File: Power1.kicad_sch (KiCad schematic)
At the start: 23 parts, among them U15 IRS2186, U16 IRS2186, U17 IRS2186, U18 Opamp_Quad

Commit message: - layout almost finished
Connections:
- net U_GH renamed U1_GH
- net U_GL renamed U1_GL
- net U_PWM_H renamed U1_PWM_H
- net U_PWM_L renamed U1_PWM_L
- net U_U renamed U1_U
- net U_VP renamed U1_VP
- net V_GH renamed V1_GH
- net V_GL renamed V1_GL
- net V_PWM_H renamed V1_PWM_H
- net V_PWM_L renamed V1_PWM_L
- net V_U renamed V1_U
- net V_VP renamed V1_VP
- net W_GH renamed W1_GH
- net W_GL renamed W1_GL
- net W_PWM_H renamed W1_PWM_H
- net W_PWM_L renamed W1_PWM_L
- net W_U renamed W1_U
- net W_VP renamed W1_VP
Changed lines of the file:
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@@
     (stroke (width 0) (type default))
   )
-  (hierarchical_label "U_GH" (shape input) (at 69.85 48.26 0) (fields_autoplaced)
+  (hierarchical_label "U1_GH" (shape input) (at 69.85 48.26 0) (fields_autoplaced)
     (effects (font (size 1.27 1.27)) (justify left))
   )
-  (hierarchical_label "U_GL" (shape input) (at 69.85 60.96 0) (fields_autoplaced)
+  (hierarchical_label "U1_GL" (shape input) (at 69.85 60.96 0) (fields_autoplaced)
     (effects (font (size 1.27 1.27)) (justify left))
   )
-  (hierarchical_label "U_PWM_L" (shape input) (at 54.61 55.88 180) (fields_autoplaced)
+  (hierarchical_label "U1_PWM_L" (shape input) (at 54.61 55.88 180) (fields_autoplaced)
     (effects (font (size 1.524 1.524)) (justify right))
   )
-  (hierarchical_label "V_PWM_L" (shape input) (at 54.61 100.33 180) (fields_autoplaced)
+  (hierarchical_label "V1_PWM_L" (shape input) (at 54.61 100.33 180) (fields_autoplaced)
     (effects (font (size 1.524 1.524)) (justify right))
   )
-  (hierarchical_label "U_U" (shape output) (at 223.52 37.465 180) (fields_autoplaced)
+  (hierarchical_label "U1_U" (shape output) (at 223.52 37.465 180) (fields_autoplaced)
     (effects (font (size 1.524 1.524)) (justify right))
   )
-  (hierarchical_label "V_GH" (shape input) (at 69.85 92.71 0) (fields_autoplaced)
+  (hierarchical_label "V1_GH" (shape input) (at 69.85 92.71 0) (fields_autoplaced)
     (effects (font (size 1.27 1.27)) (justify left))
   )
-  (hierarchical_label "V_GL" (shape input) (at 69.85 105.41 0) (fields_autoplaced)
+  (hierarchical_label "V1_GL" (shape input) (at 69.85 105.41 0) (fields_autoplaced)
     (effects (font (size 1.27 1.27)) (justify left))
   )
-  (hierarchical_label "W_VP" (shape input) (at 261.62 78.105 0) (fields_autoplaced)
+  (hierarchical_label "W1_VP" (shape input) (at 261.62 78.105 0) (fields_autoplaced)
     (effects (font (size 1.524 1.524)) (justify left))
   )
-  (hierarchical_label "V_VP" (shape input) (at 83.82 102.87 0) (fields_autoplaced)
+  (hierarchical_label "V1_VP" (shape input) (at 83.82 102.87 0) (fields_autoplaced)
     (effects (font (size 1.27 1.27)) (justify left))
   )
-  (hierarchical_label "U_VP" (shape input) (at 83.82 58.42 0) (fields_autoplaced)
+  (hierarchical_label "U1_VP" (shape input) (at 83.82 58.42 0) (fields_autoplaced)
     (effects (font (size 1.27 1.27)) (justify left))
   )
-  (hierarchical_label "U_VP" (shape input) (at 261.62 34.925 0) (fields_autoplaced)
+  (hierarchical_label "U1_VP" (shape input) (at 261.62 34.925 0) (fields_autoplaced)
     (effects (font (size 1.524 1.524)) (justify left))
   )
-  (hierarchical_label "V_VP" (shape input) (at 261.62 56.515 0) (fields_autoplaced)
+  (hierarchical_label "V1_VP" (shape input) (at 261.62 56.515 0) (fields_autoplaced)
     (effects (font (size 1.524 1.524)) (justify left))
   )
-  (hierarchical_label "V_PWM_H" (shape input) (at 54.61 97.79 180) (fields_autoplaced)
+  (hierarchical_label "V1_PWM_H" (shape input) (at 54.61 97.79 180) (fields_autoplaced)
     (effects (font (size 1.524 1.524)) (justify right))
   )
-  (hierarchical_label "W_PWM_L" (shape input) (at 54.61 144.78 180) (fields_autoplaced)
+  (hierarchical_label "W1_PWM_L" (shape input) (at 54.61 144.78 180) (fields_autoplaced)
     (effects (font (size 1.524 1.524)) (justify right))
   )
-  (hierarchical_label "U_PWM_H" (shape input) (at 54.61 53.34 180) (fields_autoplaced)
+  (hierarchical_label "U1_PWM_H" (shape input) (at 54.61 53.34 180) (fields_autoplaced)
     (effects (font (size 1.524 1.524)) (justify right))
   )
-  (hierarchical_label "W_GL" (shape input) (at 69.85 149.86 0) (fields_autoplaced)
+  (hierarchical_label "W1_GL" (shape input) (at 69.85 149.86 0) (fields_autoplaced)
     (effects (font (size 1.27 1.27)) (justify left))
   )
-  (hierarchical_label "V_U" (shape output) (at 223.52 59.055 180) (fields_autoplaced)
+  (hierarchical_label "V1_U" (shape output) (at 223.52 59.055 180) (fields_autoplaced)
     (effects (font (size 1.524 1.524)) (justify right))
   )
-  (hierarchical_label "W_PWM_H" (shape input) (at 54.61 142.24 180) (fields_autoplaced)
+  (hierarchical_label "W1_PWM_H" (shape input) (at 54.61 142.24 180) (fields_autoplaced)
     (effects (font (size 1.524 1.524)) (justify right))
   )
-  (hierarchical_label "W_U" (shape output) (at 223.52 80.645 180) (fields_autoplaced)
+  (hierarchical_label "W1_U" (shape output) (at 223.52 80.645 180) (fields_autoplaced)
     (effects (font (size 1.524 1.524)) (justify right))
   )
-  (hierarchical_label "W_GH" (shape input) (at 69.85 137.16 0) (fields_autoplaced)
+  (hierarchical_label "W1_GH" (shape input) (at 69.85 137.16 0) (fields_autoplaced)
     (effects (font (size 1.27 1.27)) (justify left))
   )
-  (hierarchical_label "W_VP" (shape input) (at 83.82 147.32 0) (fields_autoplaced)
+  (hierarchical_label "W1_VP" (shape input) (at 83.82 147.32 0) (fields_autoplaced)
     (effects (font (size 1.27 1.27)) (justify left))
   )

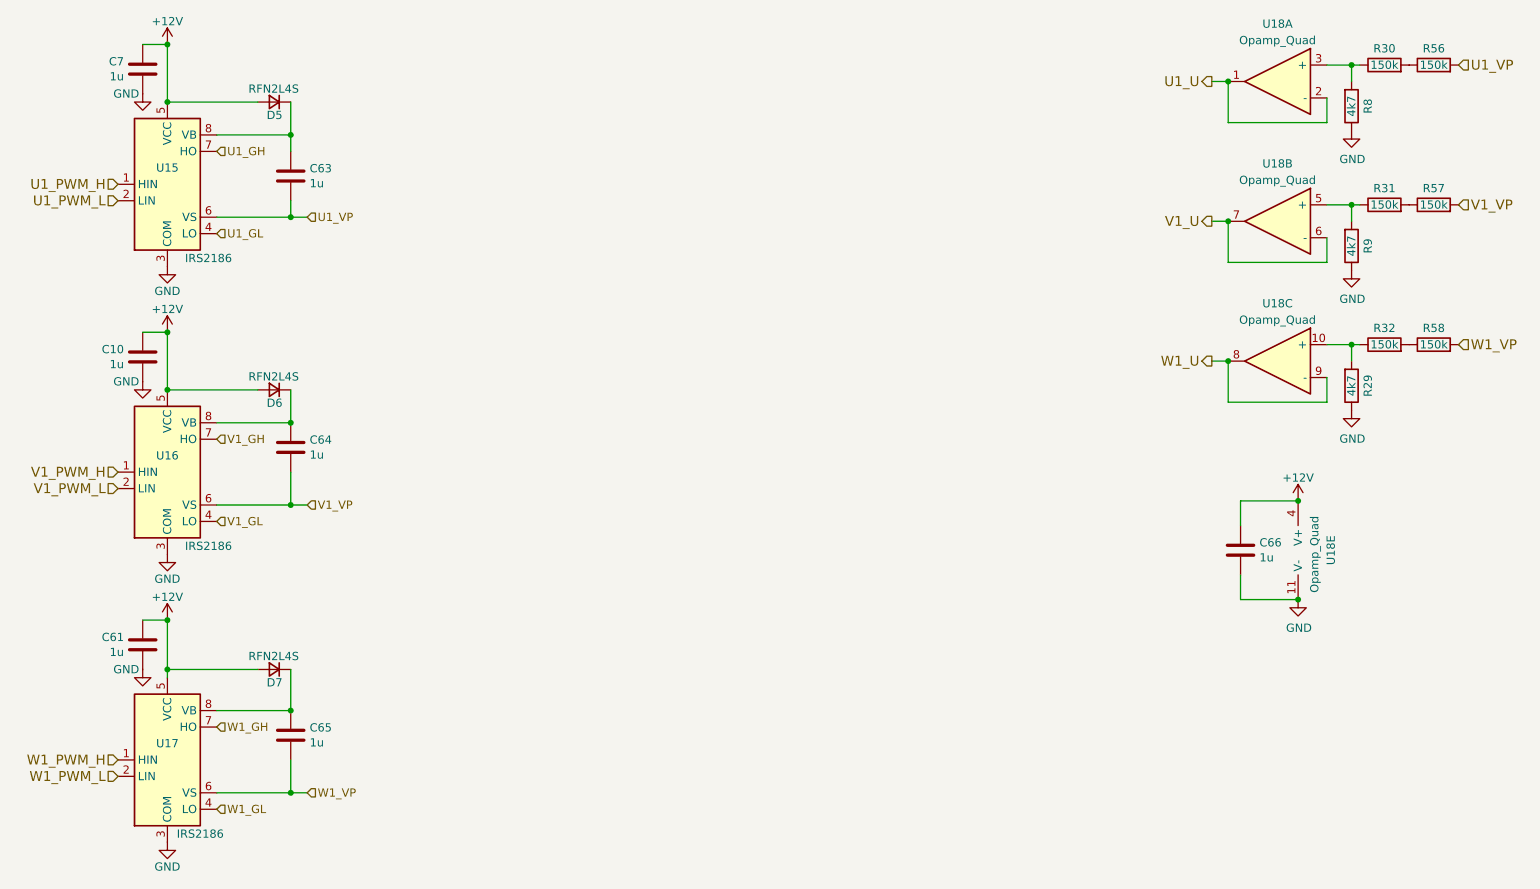
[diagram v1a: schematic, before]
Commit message: - fixed missing 3V3 trace on USB isolator
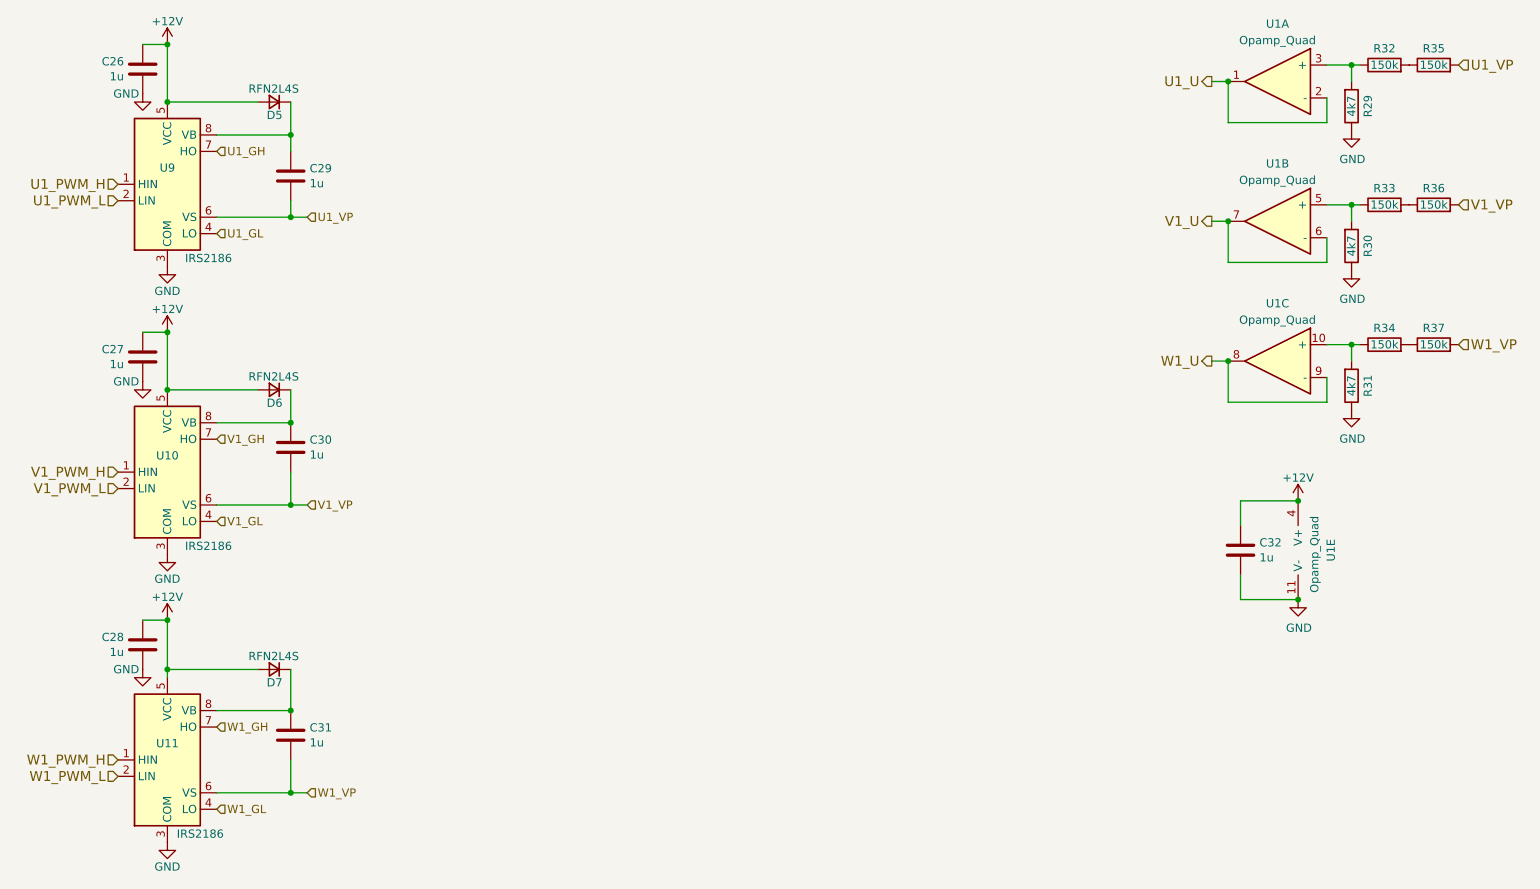
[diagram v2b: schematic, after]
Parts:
- renumbered C7 to C26, C10 to C27, C61 to C28, C63 to C29, C64 to C30, C65 to C31, C66 to C32, R8 to R29, R9 to R30, R29 to R31, R30 to R32, R31 to R33, R32 to R34, R56 to R35, R57 to R36, R58 to R37, U18 to U1, U16 to U10, U17 to U11, U15 to U9
